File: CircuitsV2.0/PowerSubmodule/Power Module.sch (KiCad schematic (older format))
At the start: 23 parts, among them IC1 LTC3895IFE#TRPBF, Q1 Si4482DY, Q2 BSC082N10LSG, Q3 BSC082N10LSG, U1 LMV321

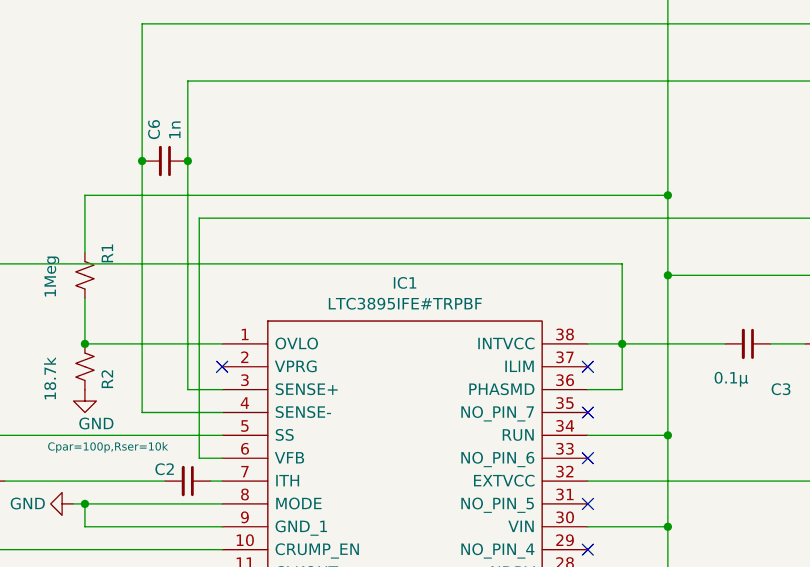
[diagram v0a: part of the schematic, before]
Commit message: Updated File structure and implemented gitignore fully for unecessary generated files. Final Schematic and PCB files added.
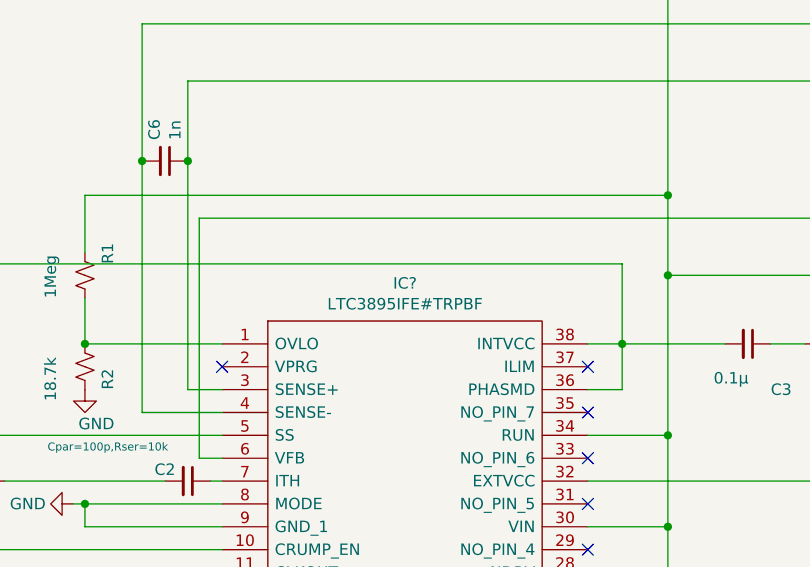
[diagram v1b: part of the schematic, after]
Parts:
- removed IC1: LTC3895IFE#TRPBF, SOP50P640X120-39N, symbol LTC3895PartLib:LTC3895IFE#TRPBF
- added IC?: LTC3895IFE#TRPBF, SOP50P640X120-39N, symbol LTC3895PartLib:LTC3895IFE#TRPBF
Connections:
- net +12V: now also IC?.32 (EXTVCC), IC?.4 (SENSE-)
- net +24V: now also IC?.30 (VIN), IC?.34 (RUN)
- net GND: now also IC?.13 (PLLIN), IC?.19 (DRVUV), IC?.8 (MODE), IC?.9 (GND_1)
- net at R1.2, R2.1: now also IC?.1 (OVLO)
- net at C5.1, L1.1, Q2.5 (D)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: now also IC?.21 (SW)
- net at Q3.4 (G): now also IC?.20 (TG)
- net at C3.2, R3.2: now also IC?.10 (CRUMP_EN), IC?.36 (PHASMD), IC?.38 (INTVCC)
- net at C5.2: now also IC?.22 (BOOST)
- net at Q2.4 (G): now also IC?.24 (BG)
- net at C6.1, L1.2, R6.2: now also IC?.3 (SENSE+)
- net at R3.1: now also IC?.14 (PGOOD)
- net at R4.1: now also IC?.17 (FREQ)
- net at R7.2, R8.1: now also IC?.6 (VFB)
- net at R5.1: now also IC?.18 (DRVSET)
- net at Q1.4 (G): now also IC?.28 (NDRV)
- net at C4.2, Q1.5 (D): now also IC?.26 (DRVCC)
- net at C2.1: now also IC?.7 (ITH)
- net at C1.1: now also IC?.5 (SS)
